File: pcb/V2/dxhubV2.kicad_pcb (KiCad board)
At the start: 2 copper layers, 75 x 75 mm, 9 parts, among them SW2 MSK12C02, U1 XL-3210SYGC, U2 XL-3210SYGC, U3 XL-3210SYGC

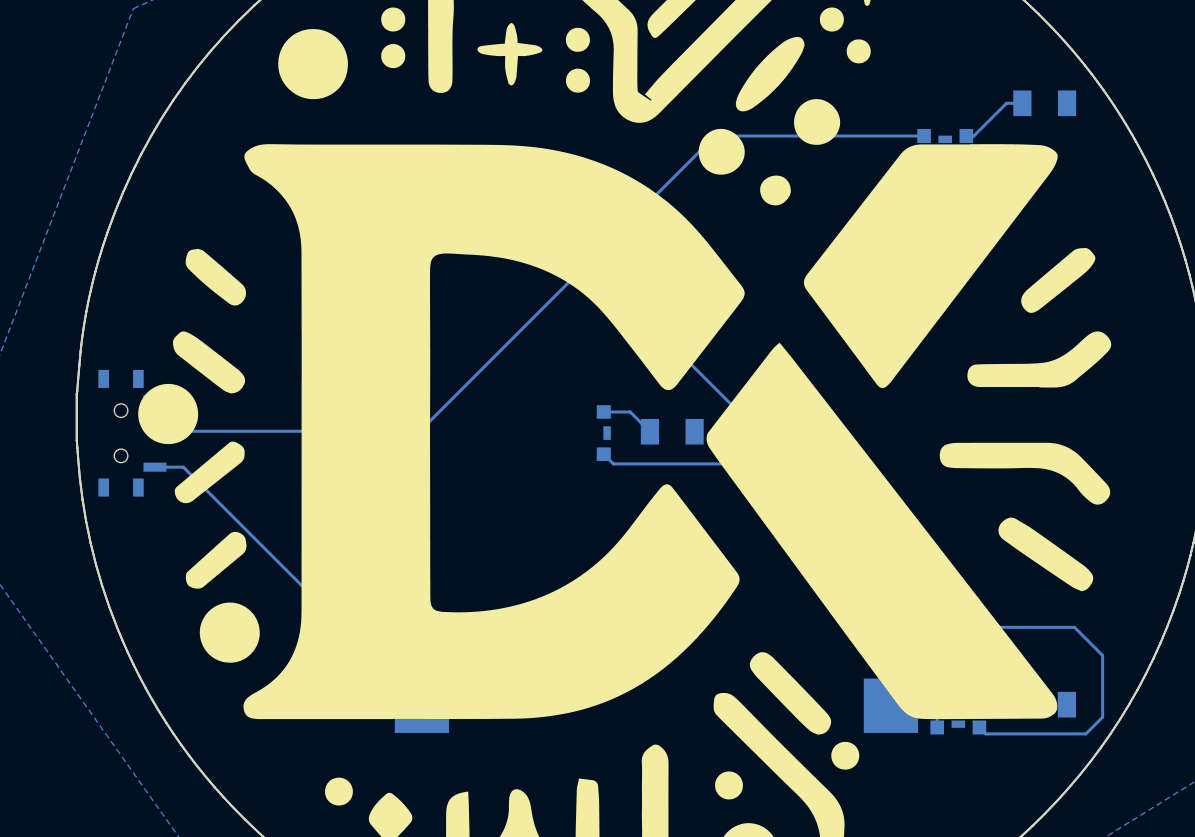
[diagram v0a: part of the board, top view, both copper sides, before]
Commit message: Ready for fab review: Modified LED footprint silk to not; new traces to match datasheet
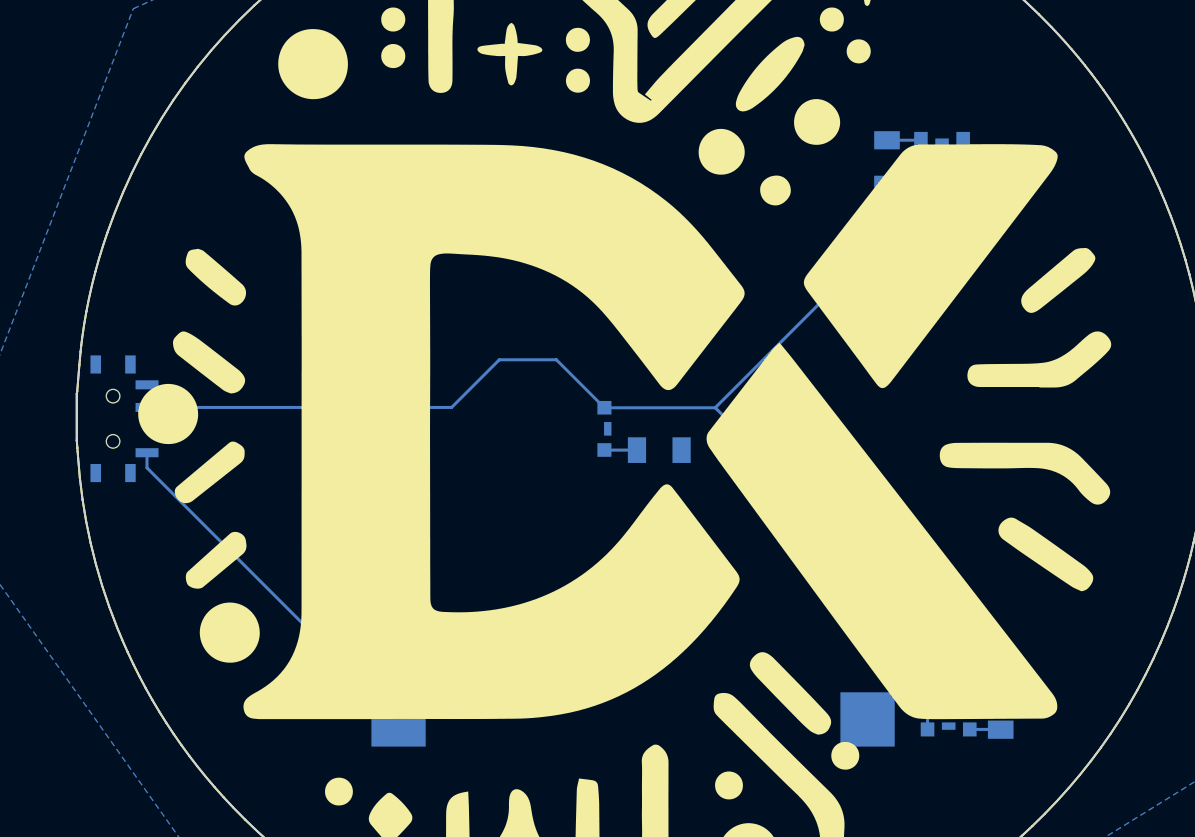
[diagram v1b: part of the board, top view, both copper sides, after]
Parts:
- removed U1, U2, U3: XL-3210SYGC, easyeda2kicad:LED-SMD_3P-L3.2-W1.5-RD_YELLOW
- added LED1: XL-3210SYGC, easyeda2kicad:LED-SMD_3P-L3.2-W1.5-RD_YELLOW, B.Cu at (70.8, 32.6)
- added LED2: XL-3210SYGC, easyeda2kicad:LED-SMD_3P-L3.2-W1.5-RD_YELLOW, B.Cu at (71.2, 71.5)
- added LED3: XL-3210SYGC, easyeda2kicad:LED-SMD_3P-L3.2-W1.5-RD_YELLOW, B.Cu at (48.5, 51.7)
- R1, R2, R3: value 1206W4J0390T5E -> 40R
- moved R1 11.2 mm to (67.1, 34.0), turned to 90 degrees
- moved R2 2.92 mm to (74.7, 70.2), turned to -90 degrees
- moved BT1 1.80 mm to (50.3, 71.0)
- moved R3 1.49 mm to (52.0, 53.1)
- moved SW1 1.10 mm to (16.4, 51.0)
- renumbered SW2 to SW1
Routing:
- net Net-(LED1-Pad1): track 129.9 -> 92.1 mm
- net Net-(LED2-Pad2): track 6.92 -> 2.06 mm
- net Net-(LED1-Pad2): track 4.62 -> 2.30 mm
- net Net-(LED3-Pad2): track 3.60 -> 2.16 mm

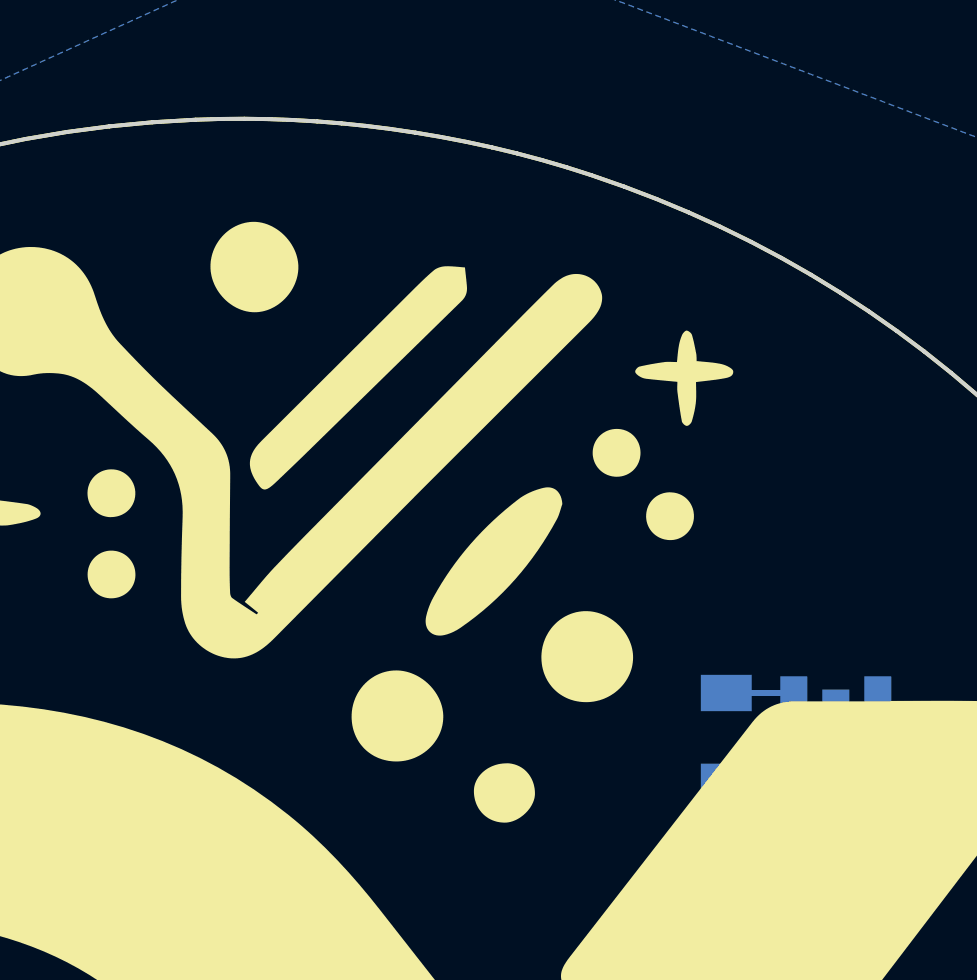
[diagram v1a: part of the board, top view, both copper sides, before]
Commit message: moved R1 to make room for pin; added hole for lanyard; increased DXHub logo size
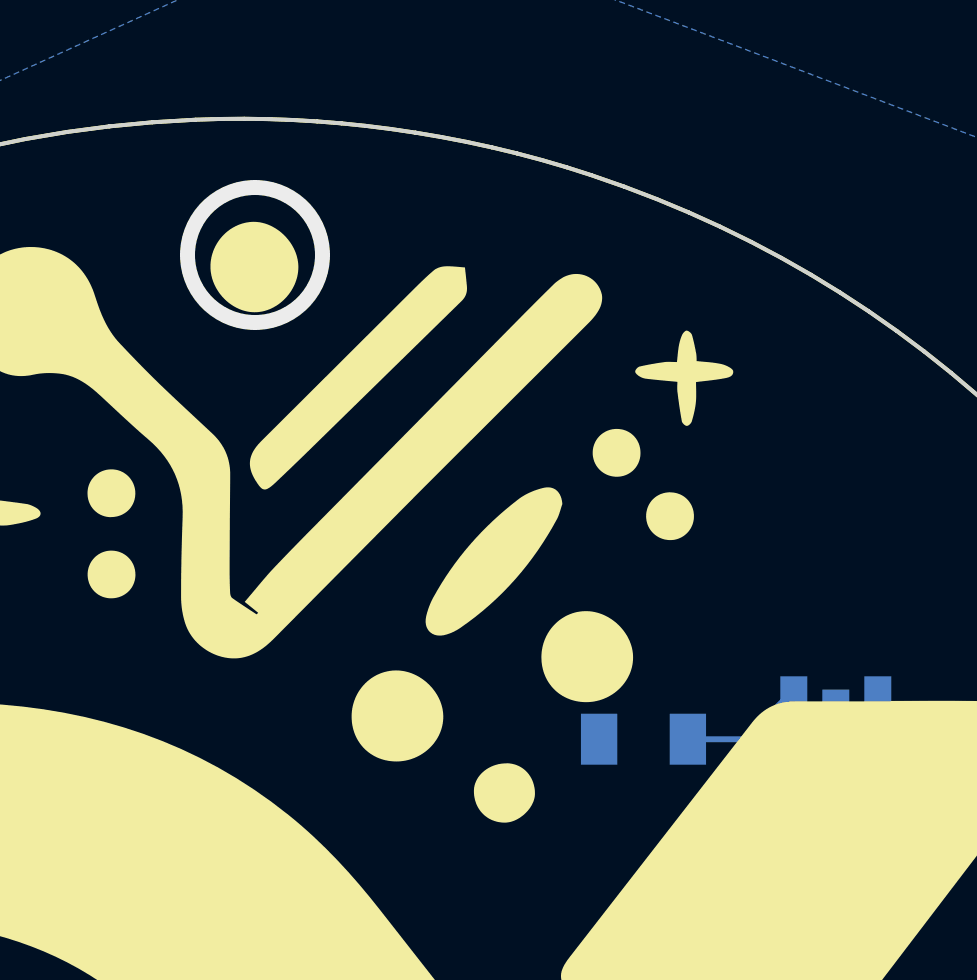
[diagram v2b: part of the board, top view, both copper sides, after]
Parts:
- moved R1 2.76 mm to (64.4, 34.1), turned to 0 degrees
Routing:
- net Net-(LED1-Pad2): track 2.30 -> 4.21 mm
- net GND: vias 0 -> 1

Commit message: This is board v0: resized logos; did some rerouting; new gerbers ready for prototype of v0.
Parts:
- moved R1 8.33 mm to (72.6, 35.1), turned to 180 degrees
- moved G*** 1.77 mm to (46.6, 30.1)
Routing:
- net Net-(LED1-Pad1): track 92.1 -> 96.9 mm
- net Net-(LED1-Pad2): track 4.21 -> 3.38 mm
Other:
- board text added: "DXHub AI Camp Badge v0"
